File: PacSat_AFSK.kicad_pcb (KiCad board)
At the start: 6 copper layers, 92 x 92 mm, 308 parts, among them J10 2118718-2, J11 Molex 73251-1153, J2 CONN_02X05, J3 2118714-2, J4 2118714-2, J5 2118714-2, J6 2118714-2, J7 2118714-2, J8 Molex 73251-1153, J9 2118714-2, P10 CONUFL001-SMD-T, P11 CONUFL001-SMD-T, P12 CONUFL001-SMD-T, P13 CONUFL001-SMD-T, P14 Conn_04x26_Pin, P2 CONUFL001-SMD-T, P3 CONUFL001-SMD-T, P4 CONUFL001-SMD-T, P5 CONUFL001-SMD-T, P6 CONUFL001-SMD-T, P7 CONUFL001-SMD-T, P9 CONUFL001-SMD-T, Q2 BSS138, Q3 DMP2037U, Q4 DMP2037U, Q5 DMP2037U, Q6 DMP2037U, Q7 DMP2037U, U10 MAX4495AAUT, U11 MAX4495AAUT, U12 MAX31331TETB+, U13 AS1016204-0108X0PWAY, U14 TCAN1044ADDFRQ1, U15 AX5043, U17 AX5043, U19 AX5043, U2 TMS570LS0914PGE, U21 AX5043, U23 AX5043, U25 QPL9547, U26 RBP-140+, U27 TQP7M9106, U28 ADL5501AKSZ-R2, U29 ADL5501AKSZ-R2, U3 CDCLVC1106, U4 TPSM828302ARDSR, U5 LP3962EMP-3.3/NOPB, U6 STWD100NYWY3F, U8 MP5073GG-P, U9 MAX4495AAUT, Y2 O 16,0-JT22CT-A-P-3,3-LF, Y3 32.768kHz

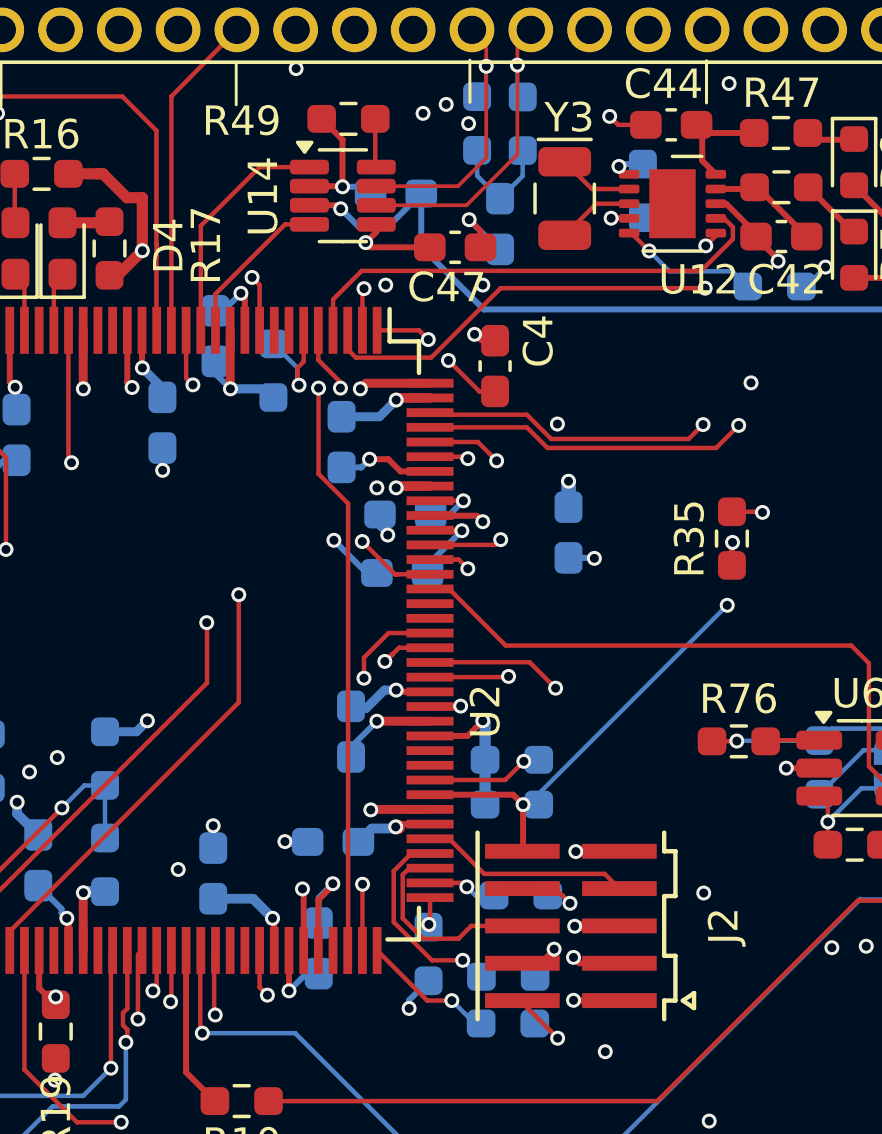
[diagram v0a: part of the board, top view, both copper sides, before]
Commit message: Fix values of a lot of parts
Make them standard, 4.1p instead of 4p1, etc.

Add a tag to a couple of ICs that didn't have a pin 1 indicator on the
board.

Signed-off-by: Corey Minyard <corey@minyard.net>
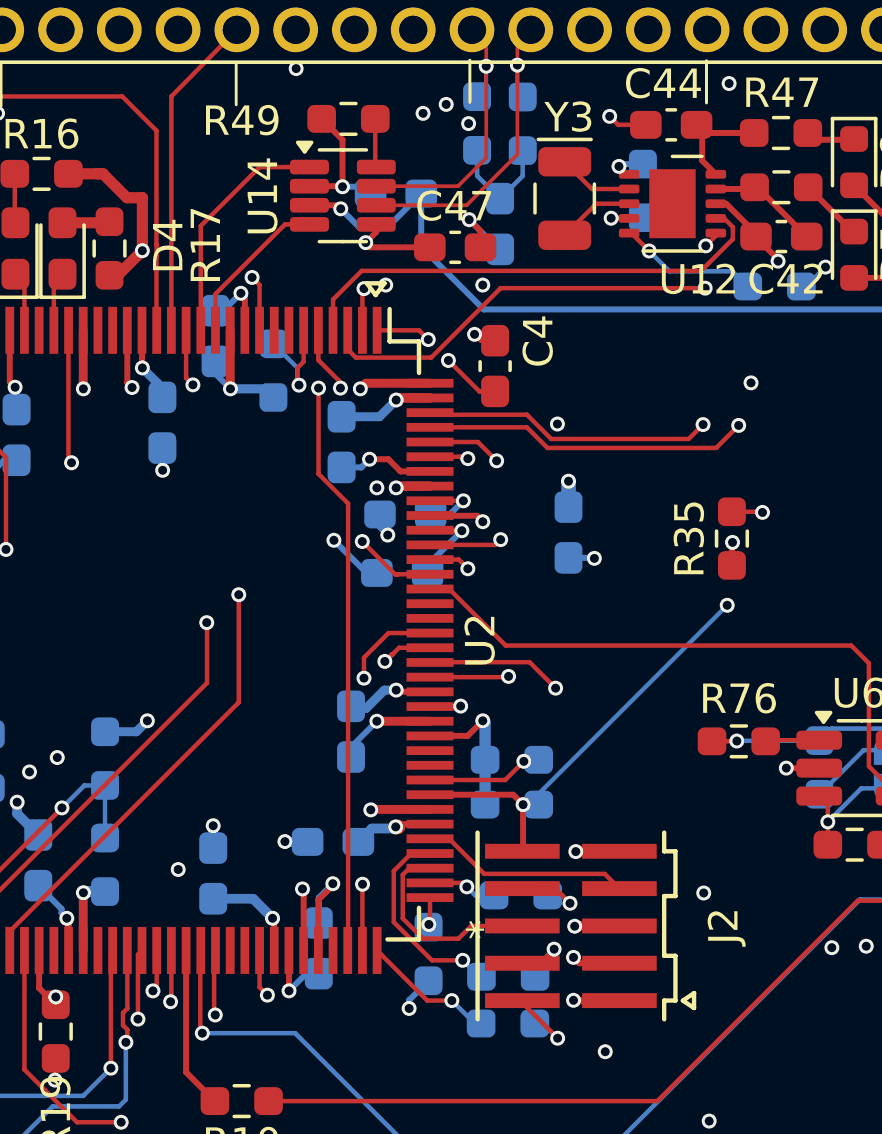
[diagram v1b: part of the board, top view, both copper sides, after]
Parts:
- C23, C24, C25, C26: value 0.1u -> 100n
- C48: value 4.7nF -> 4.7n
- C88: value 5p1 1% -> 5.1p 1%
- C90: value 5p6 1% -> 5.6p 1%
- C91, C92: value 4p3 1% -> 4.3p 1%
- L2: value 3u3 -> 3.3u
- R37, R39: value 45k8 1% -> 45.8K 1%
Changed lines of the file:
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@@
 			(plot_on_all_layers_selection 0x00000000_00000000_00000000_00000000)
 			(disableapertmacros no)
-			(usegerberextensions no)
+			(usegerberextensions yes)
 			(usegerberattributes yes)
 			(usegerberadvancedattributes yes)
@@
 			(dashed_line_gap_ratio 3.000000)
 			(svgprecision 6)
-			(plotframeref yes)
+			(plotframeref no)
 			(mode 1)
-			(useauxorigin no)
+			(useauxorigin yes)
 			(hpglpennumber 1)
 			(hpglpenspeed 20)
@@
 			(sketchdnponfab yes)
 			(crossoutdnponfab yes)
-			(subtractmaskfromsilk no)
+			(subtractmaskfromsilk yes)
 			(outputformat 1)
 			(mirror no)
@@
 		(tags "QFP 0.5")
 		(property "Reference" "U2"
-			(at 2.413 -12.446 90)
+			(at 0 -12.275 270)
 			(layer "F.SilkS")
 			(effects
@@
 		)
 		(property "Value" "TMS570LS0914PGE"
-			(at 0 12.275 90)
+			(at 0 12.275 270)
 			(layer "F.Fab")
 			(effects
@@
 		)
 		(fp_line
+			(start -12.15 -8.4)
+			(end -12.15 -9)
+			(stroke
+				(width 0.15)
+				(type solid)
+			)
+			(layer "F.SilkS")
+		)
+		(fp_line
+			(start -11.75 -8.7)
+			(end -12.15 -8.4)
+			(stroke
+				(width 0.15)
+				(type solid)
+			)
+			(layer "F.SilkS")
+		)
+		(fp_line
+			(start -12.15 -9)
+			(end -11.75 -8.7)
+			(stroke
+				(width 0.15)
+				(type solid)
+			)
+			(layer "F.SilkS")
+		)
+		(fp_line
 			(start -10.175 -9.175)
 			(end -11.275 -9.175)
@@
 			(layer "F.Fab")
 		)
+		(fp_text user "*"
+			(at 9.5 -11.25 270)
+			(unlocked yes)
+			(layer "F.SilkS")
+			(effects
+				(font
+					(size 1 1)
+					(thickness 0.1)
+				)
+				(justify left bottom)
+			)
+		)
 		(fp_text user "${REFERENCE}"
-			(at 0 0 90)
+			(at 0 0 270)
 			(layer "F.Fab")
 			(effects
@@
 		)
 		(embedded_fonts no)
-		(model ":KICAD7_3DMODEL_DIR:Package_DFN_QFN.3dshapes/QFN-48-1EP_7x7mm_P0.5mm_EP5.6x5.6mm.step"
-			(offset
-				(xyz 0 0 0)
-			)
-			(scale
-				(xyz 3 3 1)
-			)
-			(rotate
-				(xyz 0 0 90)
-			)
-		)
 	)
 	(footprint "Resistor_SMD:R_0603_1608Metric_Pad0.98x0.95mm_HandSolder"
@@
 			)
 		)
-		(property "Value" "5p1 1%"
+		(property "Value" "5.1p 1%"
 			(at 0 1.43 90)
 			(layer "F.Fab")
@@
 			)
 		)
-		(property "Value" "4p3 1%"
+		(property "Value" "4.3p 1%"
 			(at 0 1.43 90)
 			(layer "F.Fab")
@@
 			)
 		)
-		(property "Value" "45k8 1%"
+		(property "Value" "45.8K 1%"
 			(at 0 1.43 90)
 			(layer "F.Fab")
@@
 			)
 		)
-		(property "Value" "4p3 1%"
+		(property "Value" "4.3p 1%"
 			(at 0 1.43 90)
 			(layer "F.Fab")
@@
 			)
 		)
-		(property "Value" "3u3"
+		(property "Value" "3.3u"
 			(at 0 2.28 90)
 			(layer "F.Fab")
@@
 		(tags "capacitor handsolder")
 		(property "Reference" "C47"
-			(at -0.2825 1.37 0)
+			(at -0.0125 -1.38 0)
 			(layer "F.SilkS")
 			(effects
@@
 			)
 		)
-		(property "Value" "5p6 1%"
+		(property "Value" "5.6p 1%"
 			(at 0 1.43 0)
 			(layer "F.Fab")
@@
 			)
 		)
-		(property "Value" "45k8 1%"
+		(property "Value" "45.8K 1%"
 			(at 0 1.43 0)
 			(layer "F.Fab")
@@
 			)
 		)
-		(property "Value" "0.1u"
+		(property "Value" "100n"
 			(at 0 -1.43 0)
 			(layer "B.Fab")
@@
 			)
 		)
-		(property "Value" "0.1u"
+		(property "Value" "100n"
 			(at 0 -1.43 90)
 			(layer "B.Fab")
@@
 			)
 		)
-		(property "Value" "4.7nF"
+		(property "Value" "4.7n"
 			(at 0 -1.43 90)
 			(layer "B.Fab")
@@
 			)
 		)
-		(property "Value" "0.1u"
+		(property "Value" "100n"
 			(at 0 -1.43 90)
 			(layer "B.Fab")
@@
 			)
 		)
-		(property "Value" "0.1u"
+		(property "Value" "100n"
 			(at 0 -1.43 0)
 			(layer "B.Fab")

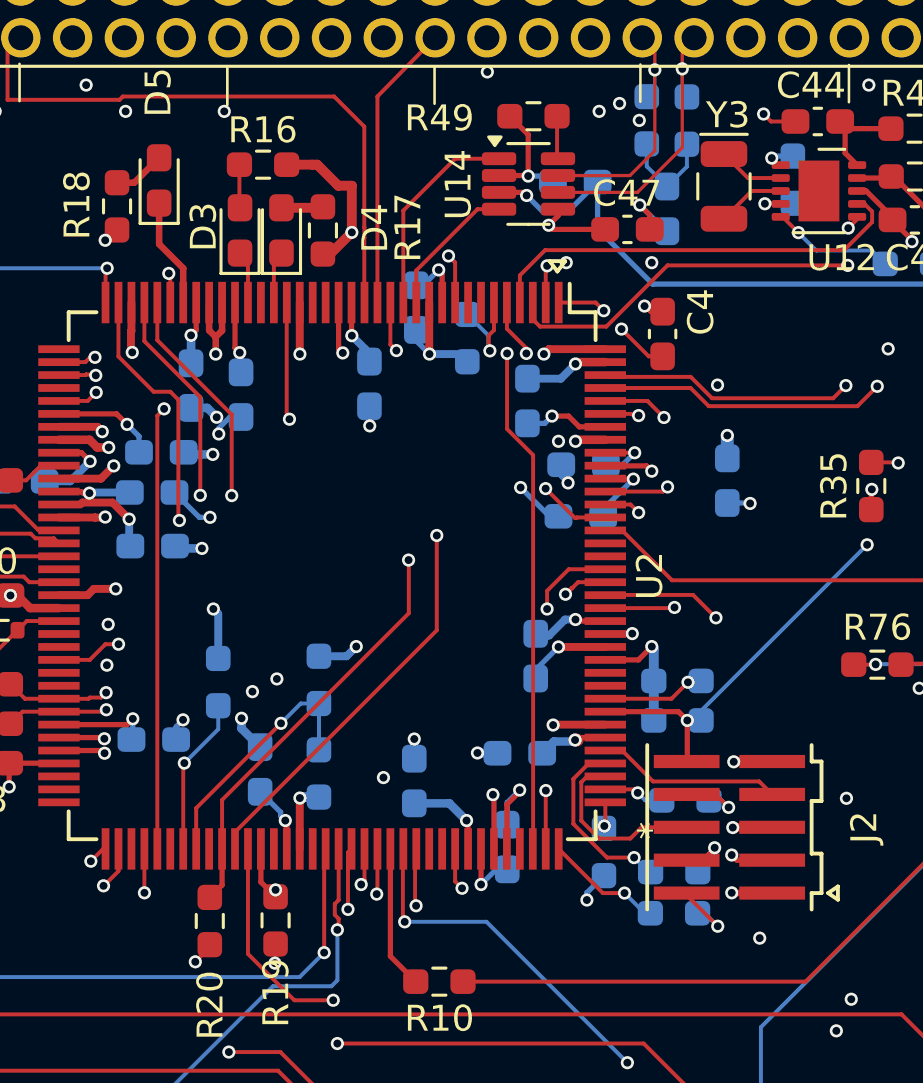
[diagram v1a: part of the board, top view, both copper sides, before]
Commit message: Move some pins around and start on the README
Move pins so that MIBSPI5 is available for use in the future.

Signed-off-by: Corey Minyard <corey@minyard.net>
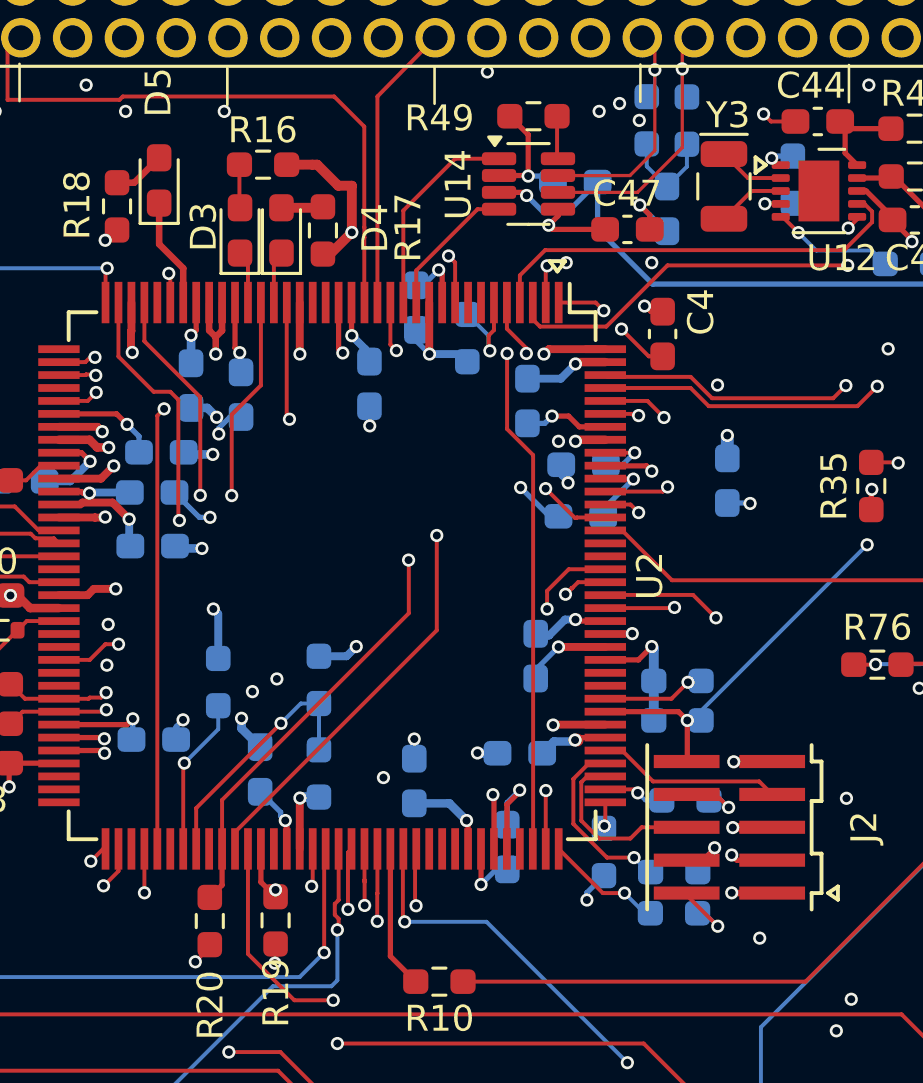
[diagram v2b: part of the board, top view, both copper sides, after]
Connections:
- U2 pad 100: AX5043_EN_TX_N -> unconnected-(U2-MIBSPI5CLK-Pad100)
- U2 pad 24: unconnected-(U2-N2HET1_3-Pad24) -> AX5043_EN_RX4_N
- U2 pad 32: AX5043_EN_RX4_N -> unconnected-(U2-MIBSPI5NCS_0-Pad32)
- U2 pad 89: unconnected-(U2-CAN1TX-Pad89) -> AX5043_EN_TX_N
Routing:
- net AX5043_EN_TX_N: track 27.1 -> 32.8 mm
- net AX5043_EN_RX4_N: track 43.4 -> 42.7 mm
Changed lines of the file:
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@@
 	(net 276 "unconnected-(U2-AD1IN_9-Pad70)")
 	(net 277 "unconnected-(U2-AD1IN_10-Pad72)")
-	(net 278 "unconnected-(U2-N2HET1_3-Pad24)")
+	(net 278 "unconnected-(U2-MIBSPI5NCS_0-Pad32)")
 	(net 279 "unconnected-(U2-AD1IN_18-Pad62)")
 	(net 280 "unconnected-(U2-AD1IN_19-Pad63)")
@@
 	(net 358 "Net-(U6-WDO_N)")
 	(net 359 "Net-(Q2-D)")
-	(net 360 "unconnected-(U2-CAN1TX-Pad89)")
+	(net 360 "unconnected-(U2-MIBSPI5CLK-Pad100)")
 	(net 361 "unconnected-(U2-N2HET1_10-Pad118)")
 	(net 362 "Net-(Q3-D)")
@@
 		(tags "QFP 0.5")
 		(property "Reference" "U2"
-			(at 0 -12.275 270)
+			(at 0 -12.275 90)
 			(layer "F.SilkS")
 			(effects
@@
 		)
 		(property "Value" "TMS570LS0914PGE"
-			(at 0 12.275 270)
+			(at 0 12.275 90)
 			(layer "F.Fab")
 			(effects
@@
 		)
 		(property "Datasheet" ""
-			(at 0 0 270)
+			(at 0 0 90)
 			(layer "F.Fab")
 			(hide yes)
@@
 		)
 		(property "Description" ""
-			(at 0 0 270)
+			(at 0 0 90)
 			(layer "F.Fab")
 			(hide yes)
@@
 			(layer "F.Fab")
 		)
-		(fp_text user "*"
-			(at 9.5 -11.25 270)
-			(unlocked yes)
-			(layer "F.SilkS")
-			(effects
-				(font
-					(size 1 1)
-					(thickness 0.1)
-				)
-				(justify left bottom)
-			)
-		)
 		(fp_text user "${REFERENCE}"
-			(at 0 0 270)
+			(at 0 0 90)
 			(layer "F.Fab")
 			(effects
@@
 			(size 1.6 0.3)
 			(layers "F.Cu" "F.Mask" "F.Paste")
-			(net 278 "unconnected-(U2-N2HET1_3-Pad24)")
+			(net 370 "AX5043_EN_RX4_N")
 			(pinfunction "N2HET1_3")
-			(pintype "bidirectional+no_connect")
+			(pintype "bidirectional")
 		)
 		(pad "25" smd rect
@@
 			(size 1.6 0.3)
 			(layers "F.Cu" "F.Mask" "F.Paste")
-			(net 370 "AX5043_EN_RX4_N")
+			(net 278 "unconnected-(U2-MIBSPI5NCS_0-Pad32)")
 			(pinfunction "MIBSPI5NCS_0")
-			(pintype "bidirectional")
+			(pintype "bidirectional+no_connect")
 		)
 		(pad "33" smd rect
@@
 			(size 1.6 0.3)
 			(layers "F.Cu" "F.Mask" "F.Paste")
-			(net 360 "unconnected-(U2-CAN1TX-Pad89)")
+			(net 371 "AX5043_EN_TX_N")
 			(pinfunction "CAN1TX")
-			(pintype "bidirectional+no_connect")
+			(pintype "bidirectional")
 		)
 		(pad "90" smd rect
@@
 			(size 1.6 0.3)
 			(layers "F.Cu" "F.Mask" "F.Paste")
-			(net 371 "AX5043_EN_TX_N")
+			(net 360 "unconnected-(U2-MIBSPI5CLK-Pad100)")
 			(pinfunction "MIBSPI5CLK")
-			(pintype "bidirectional")
+			(pintype "bidirectional+no_connect")
 		)
 		(pad "101" smd rect
@@
 		(attr smd)
 		(fp_line
+			(start -2.45 -1.3)
+			(end -2.05 -1)
+			(stroke
+				(width 0.15)
+				(type solid)
+			)
+			(layer "F.SilkS")
+		)
+		(fp_line
+			(start -2.45 -0.7)
+			(end -2.45 -1.3)
+			(stroke
+				(width 0.15)
+				(type solid)
+			)
+			(layer "F.SilkS")
+		)
+		(fp_line
+			(start -2.05 -1)
+			(end -2.45 -0.7)
+			(stroke
+				(width 0.15)
+				(type solid)
+			)
+			(layer "F.SilkS")
+		)
+		(fp_line
 			(start -1 1.61)
 			(end 1 1.61)
@@
 	(segment
 		(start 192.258 100.062)
-		(end 192.13 100.19)
+		(end 192.258 100.02)
 		(width 0.1524)
 		(layer "F.Cu")
@@
 	)
 	(segment
-		(start 192.258 100.02)
-		(end 192.258 100.062)
+		(start 161.57 113.9)
+		(end 161.57 114.4364)
 		(width 0.1524)
 		(layer "F.Cu")
@@
 	)
 	(segment
-		(start 161.57 113.9)
-		(end 161.57 114.4364)
+		(start 192.262561 100.997528)
+		(end 192.262561 100.066561)
 		(width 0.1524)
 		(layer "F.Cu")
@@
 	)
 	(segment
+		(start 192.262561 100.066561)
+		(end 192.258 100.062)
+		(width 0.1524)
+		(layer "F.Cu")
+		(net 20)
+	)
+	(segment
 		(start 175.360224 113.75)
 		(end 175.360224 114.346042)
@@
 	)
 	(via
-		(at 192.13 100.19)
+		(at 192.262561 100.997528)
 		(size 0.508)
 		(drill 0.3048)
@@
 	)
 	(segment
+		(start 192.13 101.130089)
+		(end 192.13 108.77)
+		(width 0.1524)
+		(layer "In3.Cu")
+		(net 20)
+	)
+	(segment
 		(start 175.29 108.82)
 		(end 175.34 108.77)
@@
 	)
 	(segment
+		(start 192.262561 100.997528)
+		(end 192.13 101.130089)
+		(width 0.1524)
+		(layer "In3.Cu")
+		(net 20)
+	)
+	(segment
 		(start 202.81 108.78)
 		(end 202.82 108.77)
@@
 	)
 	(segment
-		(start 192.13 100.19)
-		(end 192.13 108.77)
-		(width 0.1524)
-		(layer "In3.Cu")
-		(net 20)
-	)
-	(segment
 		(start 215.04 108.77)
 		(end 215.03 108.76)
@@
 	)
 	(segment
+		(start 192.75 101.61)
+		(end 192.75 100.54)
+		(width 0.1524)
+		(layer "F.Cu")
+		(net 21)
+	)
+	(segment
 		(start 203.31 113.6225)
 		(end 203.31 114.165)
@@
 	)
 	(segment
-		(start 192.758 98.815)
+		(start 192.75 100.54)
 		(end 192.758 100.532)
 		(width 0.1524)
@@
 	)
 	(segment
-		(start 175.860224 113.709776)
-		(end 175.860224 114.346042)
+		(start 192.758 100.532)
+		(end 192.758 98.815)
 		(width 0.1524)
 		(layer "F.Cu")
@@
 	)
 	(segment
-		(start 176.055283 113.553528)
-		(end 176.016472 113.553528)
+		(start 175.860224 113.709776)
+		(end 175.860224 114.346042)
 		(width 0.1524)
 		(layer "F.Cu")
@@
 	)
 	(segment
-		(start 192.758 100.532)
-		(end 192.73 100.56)
+		(start 176.055283 113.553528)
+		(end 176.016472 113.553528)
 		(width 0.1524)
 		(layer "F.Cu")
@@
 	)
 	(via
-		(at 192.73 100.56)
+		(at 192.75 101.61)
 		(size 0.508)
 		(drill 0.3048)
@@
 	)
 	(segment
+		(start 192.75 101.61)
+		(end 192.73 101.63)
+		(width 0.1524)
+		(layer "In3.Cu")
+		(net 21)
+	)
+	(segment
+		(start 192.73 101.63)
+		(end 192.73 109.46)
+		(width 0.1524)
+		(layer "In3.Cu")
+		(net 21)
+	)
+	(segment
 		(start 203.50625 113.42625)
 		(end 203.50625 109.48625)
@@
 	)
 	(segment
-		(start 192.73 100.56)
-		(end 192.73 109.46)
-		(width 0.1524)
-		(layer "In3.Cu")
-		(net 21)
-	)
-	(segment
 		(start 189.51 109.47)
 		(end 189.5 109.46)
@@
 	)
 	(segment
-		(start 184.258 79.169086)
-		(end 187.13 82.041086)
-		(width 0.1524)
-		(layer "F.Cu")
-		(net 370)
-	)
-	(segment
-		(start 184.258 77.715)
-		(end 184.258 79.169086)
+		(start 187.13 82.041086)
+		(end 188.258 80.913086)
 		(width 0.1524)
 		(layer "F.Cu")
@@
 		(net 370)
 	)
+	(segment
+		(start 188.258 80.913086)
+		(end 188.258 77.715)
+		(width 0.1524)
+		(layer "F.Cu")
+		(net 370)
+	)
 	(via
 		(at 187.02 106.66)
@@
 	)
 	(segment
-		(start 195.758 98.815)
-		(end 195.758 100.068)
+		(start 190.258 100.2194)
+		(end 190.2174 100.26)
 		(width 0.1524)
 		(layer "F.Cu")
@@
 	)
 	(segment
-		(start 195.758 100.068)
-		(end 196.025 100.335)
+		(start 190.258 98.815)
+		(end 190.258 100.2194)
 		(width 0.1524)
 		(layer "F.Cu")
@@
 	)
 	(via
-		(at 196.025 100.335)
+		(at 190.2174 100.26)
 		(size 0.508)
 		(drill 0.3048)
@@
 	)
 	(segment
-		(start 219.76 100.77)
-		(end 219.2028 100.77)
+		(start 197.0064 101.3164)
+		(end 218.6564 101.3164)
 		(width 0.1524)
 		(layer "In2.Cu")
@@
 	)
 	(segment
-		(start 218.6564 101.3164)
+		(start 195.95 100.26)
 		(end 197.0064 101.3164)
 		(width 0.1524)
@@
 	)
 	(segment
-		(start 197.0064 101.3164)
-		(end 196.025 100.335)
+		(start 218.6564 101.3164)
+		(end 219.2028 100.77)
+		(width 0.1524)
+		(layer "In2.Cu")
+		(net 371)
+	)
+	(segment
+		(start 190.2174 100.26)
+		(end 195.95 100.26)
 		(width 0.1524)
 		(layer "In2.Cu")
@@
 	(segment
 		(start 219.2028 100.77)
-		(end 218.6564 101.3164)
+		(end 219.76 100.77)
 		(width 0.1524)
 		(layer "In2.Cu")

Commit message: Minor adjustments to values and impedance match simulation
Signed-off-by: Corey Minyard <corey@minyard.net>
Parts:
- D2: value LED -> BLUE LED
- D3: value RED -> RED LED
- D4: value YEL -> YELLOW LED
- D5: value GRN -> GREEN LED
- J2: value CONN_02X05 -> FTSH-105-01-L-DV-K
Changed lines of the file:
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@@
 			)
 		)
-		(property "Value" "RED"
+		(property "Value" "RED LED"
 			(at 0 1.43 90)
 			(layer "F.Fab")
@@
 			)
 		)
-		(property "Value" "YEL"
+		(property "Value" "YELLOW LED"
 			(at 0 1.43 90)
 			(layer "F.Fab")
@@
 			)
 		)
-		(property "Value" "GRN"
+		(property "Value" "GREEN LED"
 			(at 0 1.43 90)
 			(layer "F.Fab")
@@
 			)
 		)
-		(property "Value" "CONN_02X05"
+		(property "Value" "FTSH-105-01-L-DV-K"
 			(at 0 -5.08 90)
 			(layer "F.Fab")
@@
 			)
 		)
-		(property "Description" ""
+		(property "Description" "CONN_02X05"
 			(at 0 0 90)
 			(layer "F.Fab")
@@
 			)
 		)
-		(property "Value" "LED"
+		(property "Value" "BLUE LED"
 			(at 0 1.43 90)
 			(layer "F.Fab")
